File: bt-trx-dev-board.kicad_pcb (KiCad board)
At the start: 2 copper layers, 78 x 68 mm, 55 parts, among them J1 RJ45, J2 PTT_BUTTON, J3 AudioJack3, J5 PTT_SELECT, J6 I2C, J7 Conn_01x02, SW1 SW_Push, U1 SILabs_WT32i, U3 ESP32-DEVKIT

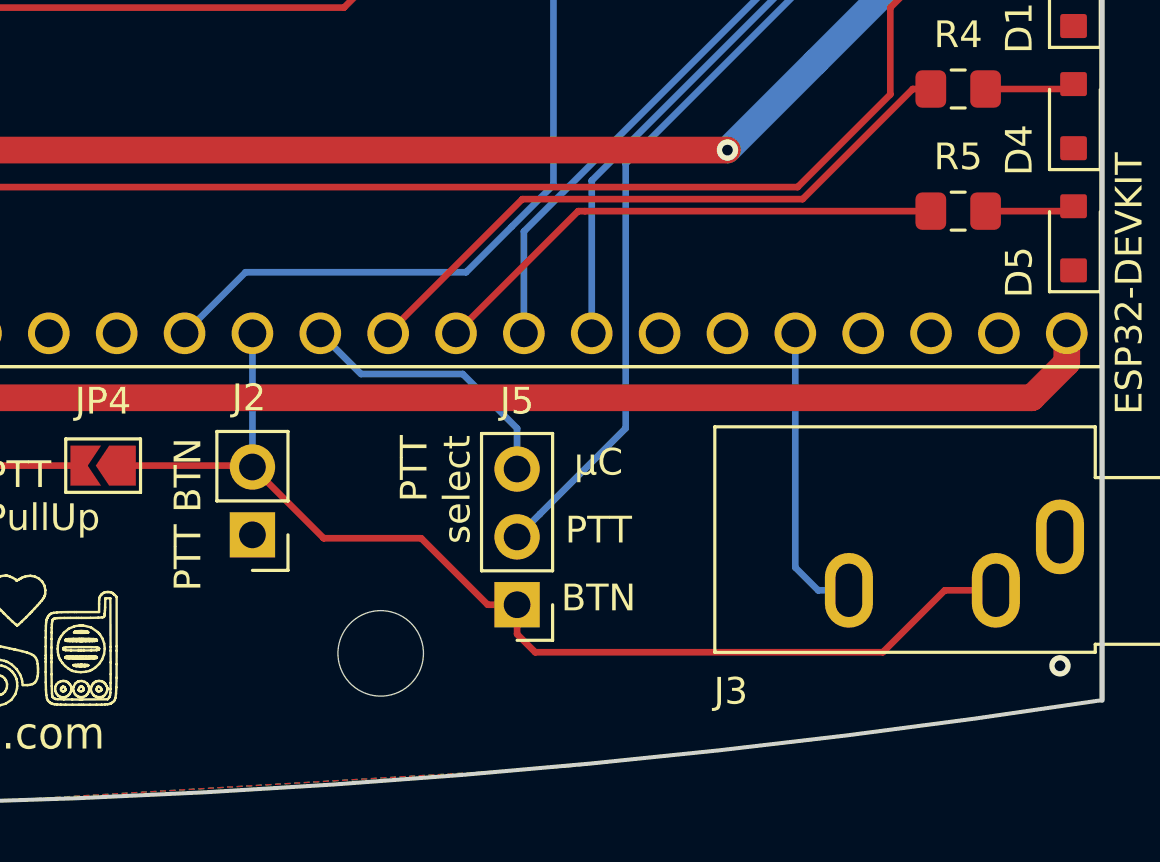
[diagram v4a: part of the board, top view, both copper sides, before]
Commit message: [#17] Add PTT_LED to J2 and move J2 near/behind J3
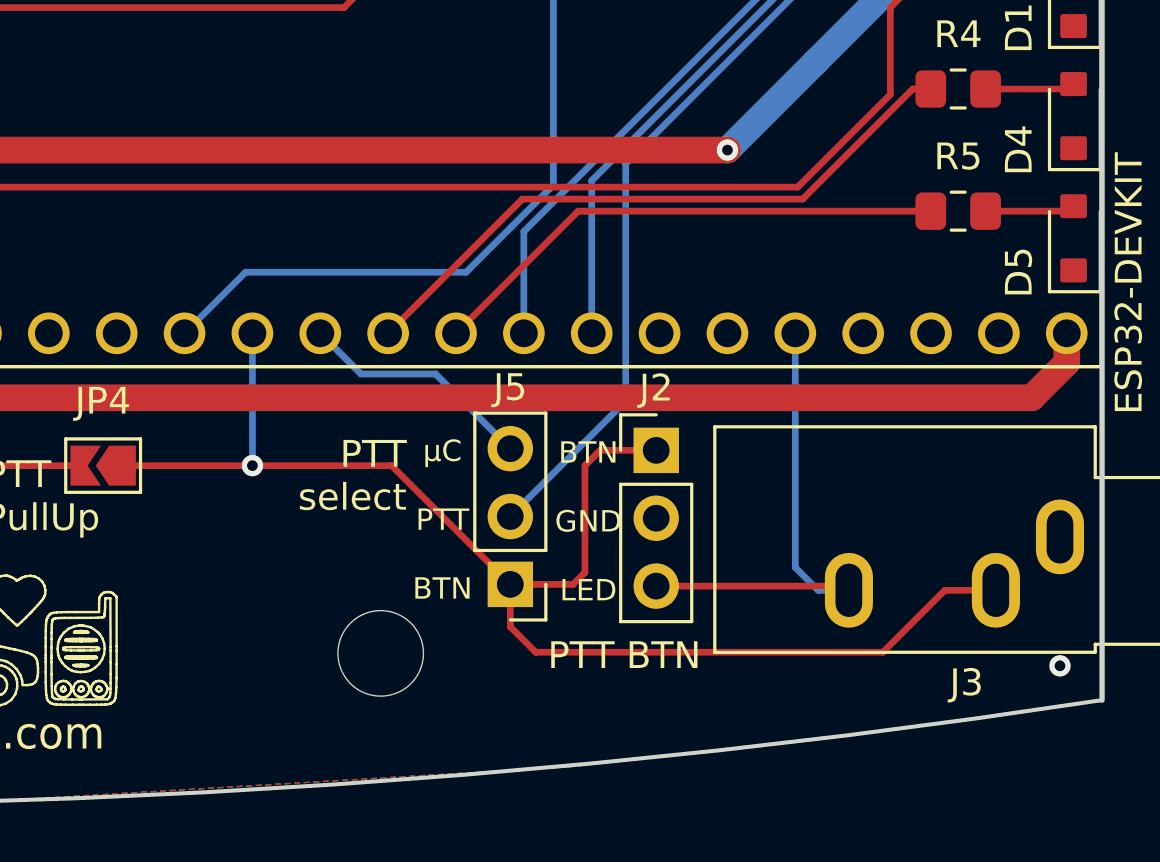
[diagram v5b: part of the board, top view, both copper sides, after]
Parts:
- J2: footprint Connector_PinHeader_2.54mm:PinHeader_1x02_P2.54mm_Vertical -> Connector_PinHeader_2.54mm:PinHeader_1x03_P2.54mm_Vertical
- J3: value AudioJack3 -> PTT_CON
- moved J2 15.4 mm to (181.7, 120.0), turned to 0 degrees
- moved J5 0.80 mm to (176.3, 125.0)
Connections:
- J2 pad 1: GND -> /PTT_BUTTON
- J2 pad 2: /PTT_BUTTON -> GND
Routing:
- net /PTT_BUTTON: track 42.2 -> 52.5 mm, vias 0 -> 1
- net /UC_PTT_LED: track 11.1 -> 18.6 mm
- net /UC_PTT_OUT: track 10.4 -> 8.90 mm
- net /PTT: track 51.0 -> 50.3 mm
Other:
- board text added: "BTN GND LED"
- board text added: "µC PTT BTN"
- board text removed: "BTN"
- board text removed: "PTT"
- board text removed: "µC"

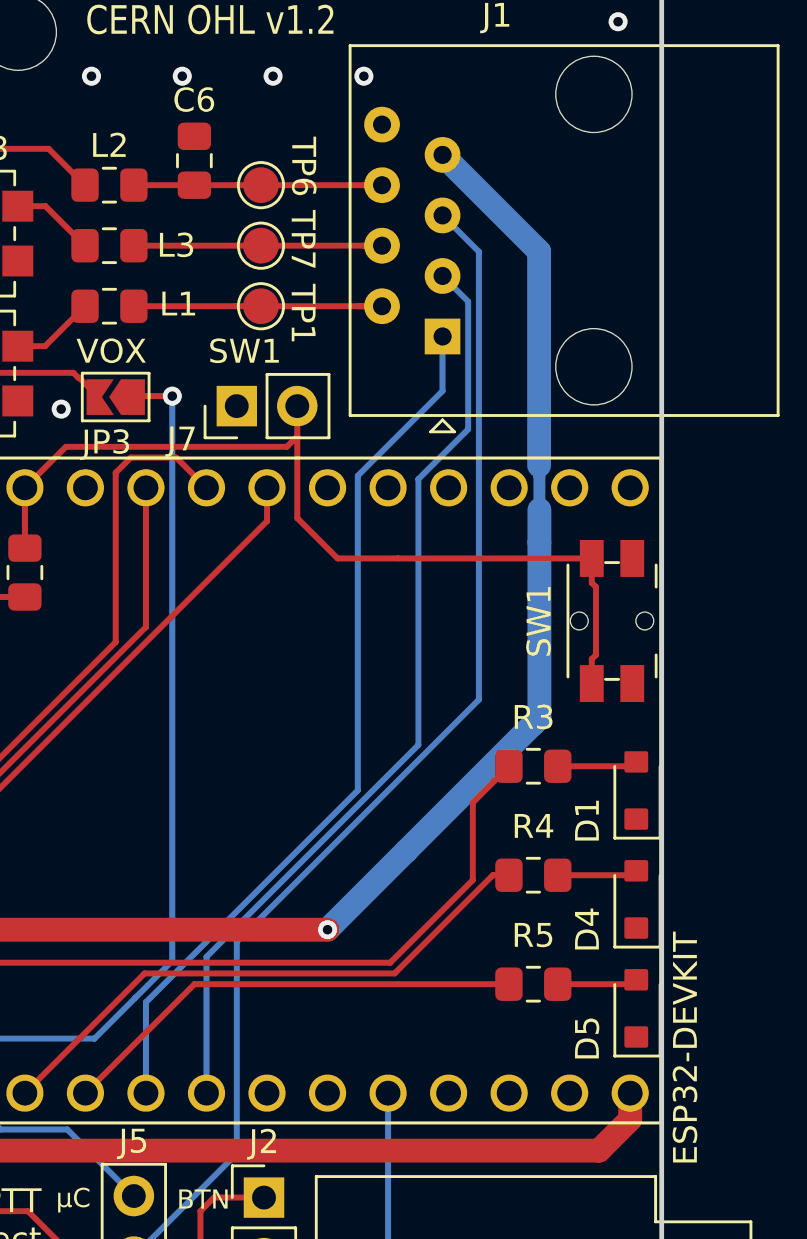
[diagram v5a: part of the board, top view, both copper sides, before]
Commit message: [#18] Changed SW1 from SMD to TH
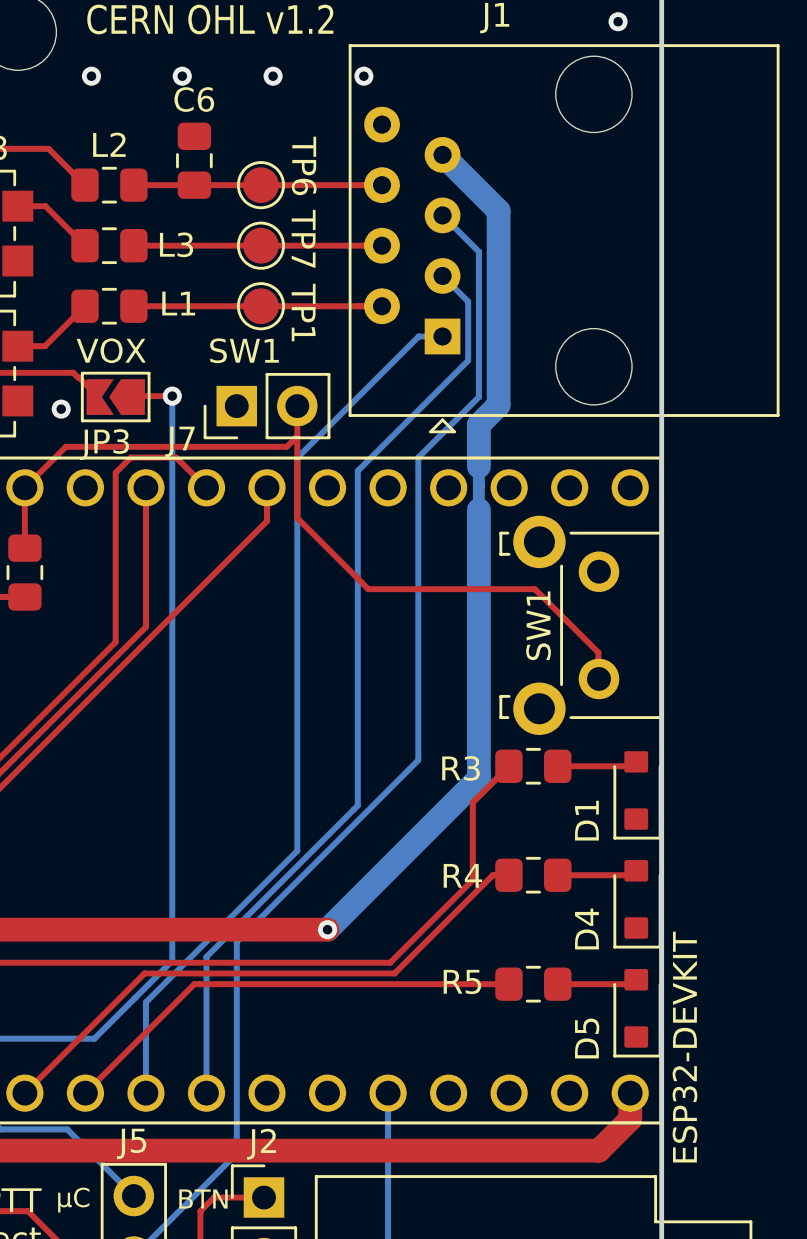
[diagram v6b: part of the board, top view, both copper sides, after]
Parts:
- SW1: footprint Button_Switch_SMD:Panasonic_EVQPUL_EVQPUC -> Button_Switch_THT:SW_Tactile_SKHH_Angled
- moved SW1 2.14 mm to (195.8, 93.7)
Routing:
- net /Microcontroller/BTN0: track 37.8 -> 35.7 mm
- net /V_IN: track 81.1 -> 79.5 mm
- net /CAT_TX: track 36.9 -> 37.5 mm

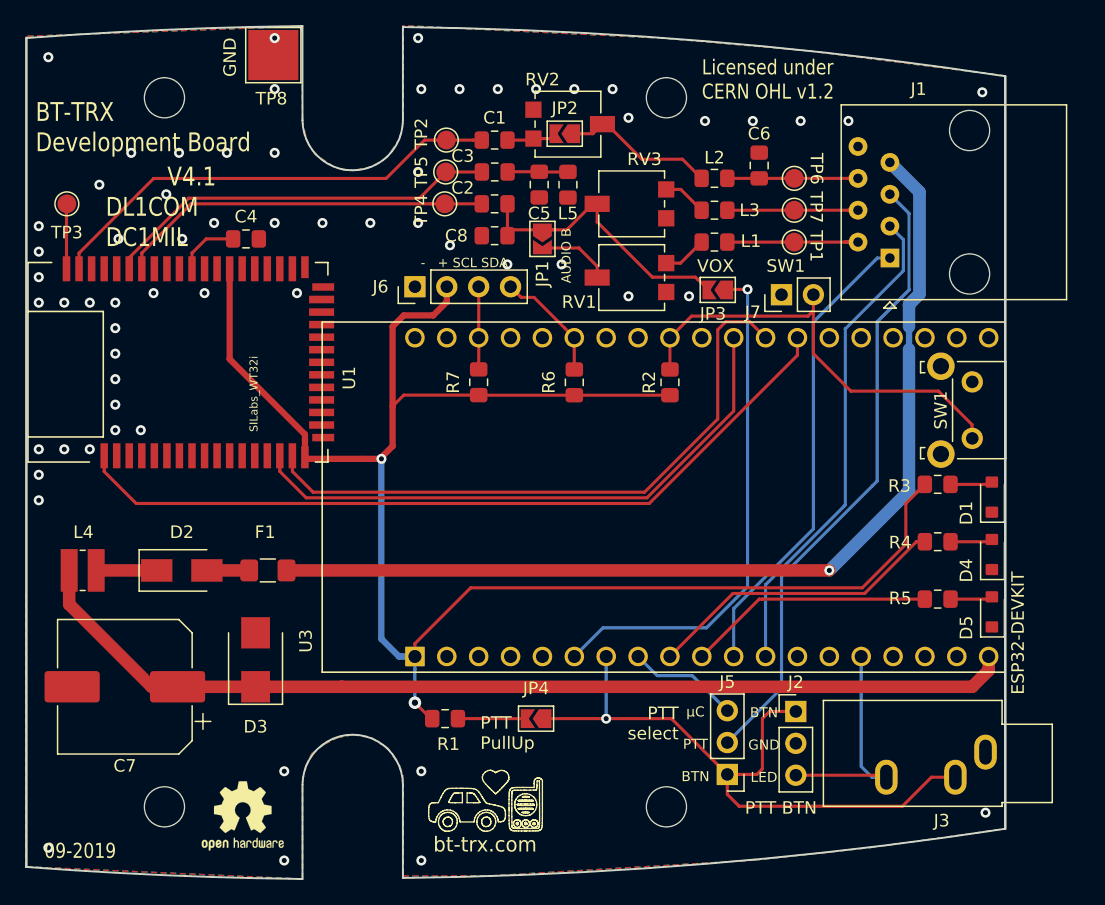
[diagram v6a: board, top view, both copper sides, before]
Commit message: Reworked PCB [#19][#21][#22][#23]
* Reworked PCB with new v5.0 schematic
* Fixed position of mounting holes
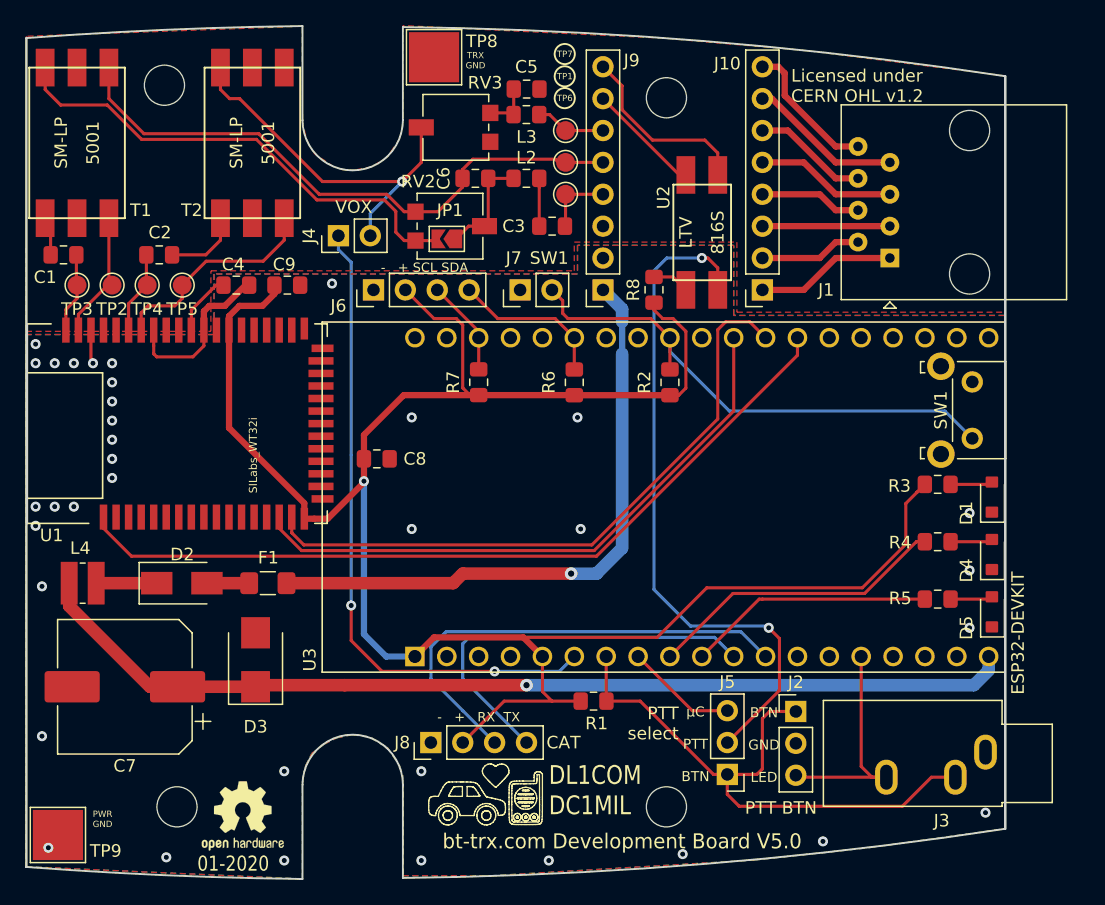
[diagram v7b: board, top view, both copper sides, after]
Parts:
- removed JP2: BYPASS, Jumper:SolderJumper-2_P1.3mm_Open_TrianglePad1.0x1.5mm
- removed JP3: VOX, Jumper:SolderJumper-2_P1.3mm_Open_TrianglePad1.0x1.5mm
- removed JP4: EN_PTT_PULLUP, Jumper:SolderJumper-2_P1.3mm_Open_TrianglePad1.0x1.5mm
- removed L1, L5: 100nH, Inductor_SMD:L_0805_2012Metric_Pad1.15x1.40mm_HandSolder
- removed RV1: 10k, Potentiometer_SMD:Potentiometer_Vishay_TS53YL_Vertical
- added C9: 100nF, Capacitor_SMD:C_0805_2012Metric_Pad1.15x1.40mm_HandSolder, F.Cu at (141.2, 86.0)
- added J10: Conn_01x08, Connector_PinSocket_2.54mm:PinSocket_1x08_P2.54mm_Vertical, F.Cu at (179.1, 86.4)
- added J4: Conn_01x02, Connector_PinHeader_2.54mm:PinHeader_1x02_P2.54mm_Vertical, F.Cu at (145.3, 82.0)
- added J8: I2C, Connector_PinHeader_2.54mm:PinHeader_1x04_P2.54mm_Vertical, F.Cu at (152.7, 122.4)
- added J9: Conn_01x08, Connector_PinSocket_2.54mm:PinSocket_1x08_P2.54mm_Vertical, F.Cu at (166.4, 86.4)
- added R8: 220R, Resistor_SMD:R_0805_2012Metric_Pad1.15x1.40mm_HandSolder, F.Cu at (170.4, 86.4)
- added T1: SM-LP-5001, bourns:SM-LP-5001, F.Cu at (121.9, 80.6)
- added T2: SM-LP-5001, bourns:SM-LP-5001, F.Cu at (135.9, 80.6)
- added TP9: PWR_GND, TestPoint:TestPoint_Pad_4.0x4.0mm, F.Cu at (122.9, 129.8)
- added U2: LTV-816S, liteon:LTV-816S, F.Cu at (173.0, 86.4)
- C8: value 15pF -> 100nF
- J5: value PTT_SELECT -> PTT_SEL
- JP1: value AUDIO_B -> BYPASS
- RV2, RV3: value 10k -> 5k
- TP1: value AUDIO_IN_B -> MIC_GND
- TP2: value SP_LN -> A_OUT_LN
- TP3: value SP_LP -> A_OUT_LP
- TP4: value MIC_LP -> A_IN_LP
- TP5: value MIC_LN -> A_IN_LN
- TP7: value AUDIO_IN_A -> AUDIO_IN
- TP8: value GND -> TRX_GND
- moved C1 35.5 mm to (123.4, 83.6), turned to 0 degrees
- moved TP2 29.0 mm to (127.3, 86.0)
- moved C2 27.0 mm to (131.0, 83.6)
- moved TP4 24.6 mm to (130.0, 86.0)
- moved TP5 22.9 mm to (132.8, 86.0)
- moved C6 22.6 mm to (156.2, 77.5), turned to 180 degrees
- moved J7 20.8 mm to (159.8, 86.4)
- moved C8 20.1 mm to (148.3, 99.8)
- moved TP7 19.3 mm to (163.4, 73.7)
- moved TP1 19.3 mm to (163.4, 76.2)
- moved TP6 18.3 mm to (163.4, 78.7)
- moved L3 16.8 mm to (160.3, 72.4)
- moved RV3 15.3 mm to (154.6, 73.4)
- moved L2 15.0 mm to (160.3, 77.5)
- moved TP8 12.8 mm to (152.9, 67.8)
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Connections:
- net /MIC_BIAS renamed Net-(C4-Pad2)
- C1 pad 2: /SPK_LN -> /A_OUT_LP
- C2 pad 1: AUDIO_B -> Net-(C2-Pad1)
- C2 pad 2: /MIC_LP -> /A_IN_LN
- C3 pad 1: Net-(C3-Pad1) -> /AUDIO_OUT_MIC
- C3 pad 2: /MIC_LN -> Net-(C3-Pad2)
- C4 pad 1: GND -> GNDPWR
- C5 pad 1: Net-(C3-Pad1) -> Net-(C5-Pad1)
- C6 pad 1: /AUDIO_OUT -> Net-(C6-Pad1)
- C6 pad 2: GND -> GNDA
- C7 pad 2: GND -> GNDPWR
- C8 pad 1: AUDIO_B -> GNDPWR
- C8 pad 2: GND -> +3V3
- D1 pad 1: GND -> GNDPWR
- D3 pad 2: GND -> GNDPWR
- D4 pad 1: GND -> GNDPWR
- D5 pad 1: GND -> GNDPWR
- J1 pad 1: /CAT_TX -> /1
- J1 pad 2: /AUDIO_IN_B -> /2
- J1 pad 3: /CAT_RX -> /3
- J1 pad 4: /AUDIO_IN_A -> /4
- J1 pad 5: /PTT -> /5
- J1 pad 6: /AUDIO_OUT -> /6
- J1 pad 7: /V_IN -> /7
- J1 pad 8: GND -> /8
- J2 pad 2: GND -> GNDPWR
- J3 pad S: GND -> GNDPWR
- J5 pad 2: /PTT -> Net-(J5-Pad2)
- J6 pad 1: GND -> GNDPWR
- J7 pad 1: GND -> GNDPWR
- JP1 pad 1: AUDIO_B -> Net-(C6-Pad1)
- L2 pad 1: Net-(JP2-Pad1) -> Net-(C6-Pad1)
- L2 pad 2: /AUDIO_OUT -> Net-(C3-Pad2)
- L3 pad 1: Net-(L3-Pad1) -> Net-(C5-Pad1)
- L3 pad 2: /AUDIO_IN_A -> /AUDIO_IN_SPK
- R1 pad 1: +3V3 -> /PTT_BUTTON
- R1 pad 2: Net-(JP4-Pad2) -> +3V3
- RV2 pad 1: Net-(C1-Pad1) -> Net-(JP1-Pad2)
- RV2 pad 2: Net-(JP2-Pad1) -> Net-(C6-Pad1)
- RV2 pad 3: GND -> GNDA
- RV3 pad 1: Net-(L3-Pad1) -> Net-(C5-Pad1)
- RV3 pad 2: AUDIO_B -> /VOX
- SW1 pad 1: GND -> GNDPWR
- TP1 pad 1: /AUDIO_IN_B -> GNDA
- TP2 pad 1: /SPK_LN -> /A_OUT_LN
- TP3 pad 1: /SPK_LP -> /A_OUT_LP
- TP4 pad 1: /MIC_LP -> /A_IN_LN
- TP5 pad 1: /MIC_LN -> /A_IN_LP
- TP6 pad 1: /AUDIO_OUT -> /AUDIO_OUT_MIC
- TP7 pad 1: /AUDIO_IN_A -> /AUDIO_IN_SPK
- U1 pad 18: GND -> GNDPWR
- U1 pad 2: GND -> GNDPWR
- U1 pad 3: GND -> GNDPWR
- U1 pad 31: GND -> GNDPWR
- U1 pad 39: GND -> GNDPWR
- U1 pad 4: GND -> GNDPWR
- U1 pad 43: GND -> GNDPWR
- U1 pad 44: /MIC_LP -> /A_IN_LP
- U1 pad 45: /MIC_LN -> /A_IN_LN
- U1 pad 48: GND -> GNDPWR
- U1 pad 49: /SPK_LN -> /A_OUT_LN
- U1 pad 50: /SPK_LP -> /A_OUT_LP
- U3 pad 11: /CAT_TX -> /Microcontroller/CAT_TX
- U3 pad 12: /CAT_RX -> /Microcontroller/CAT_RX
- U3 pad 14: GND -> GNDPWR
- U3 pad 20: GND -> GNDPWR
- U3 pad 26: GND -> GNDPWR
- U3 pad 5: GND -> +3V3
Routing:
- net Net-(J5-Pad2): track 0.00 -> 54.6 mm, vias 0 -> 2
- net GNDA: track 0.00 -> 48.2 mm
- net /PTT: track 50.3 -> 9.12 mm
- net /CAT_RX: track 39.3 -> 0.00 mm
- net /Microcontroller/CAT_RX: track 0.00 -> 37.7 mm
- net /CAT_TX: track 37.5 -> 0.00 mm
- net /SPK_LN: track 37.1 -> 0.00 mm
- net Net-(JP1-Pad2): track 5.86 -> 39.0 mm
- net /Microcontroller/CAT_TX: track 0.00 -> 32.4 mm
- net /MIC_LN: track 31.8 -> 0.00 mm
- net /V_IN: track 79.5 -> 49.1 mm
- net /MIC_LP: track 30.0 -> 0.00 mm
- net /VOX: track 0.00 -> 29.6 mm, vias 0 -> 1
- net +3V3: track 135.3 -> 163.9 mm, vias 2 -> 1
- net AUDIO_B: track 23.3 -> 0.00 mm
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- added copper zone on B.Cu, net GNDPWR
- added copper zone on F.Cu, net GNDPWR
- removed copper zone on B.Cu, net GND
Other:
- board text added: "- + RX TX"
- board text added: "01-2020"
- board text added: "CAT"
- board text added: "DL1COM DC1MIL"
- board text added: "PWR GND"
- board text added: "TRX GND"
- board text added: "bt-trx.com Development Board V5.0"
- board text removed: "09-2019"
- board text removed: "AUDIO B"
- board text removed: "BT-TRX Development Board"
- board text removed: "GND"
- board text removed: "PTT PullUp"
- board text removed: "V4.1 DL1COM DC1MIL"
- board text removed: "bt-trx.com"
